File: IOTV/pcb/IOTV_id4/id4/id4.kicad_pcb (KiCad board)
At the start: 2 copper layers, 35.6 x 53.3 mm, 7 parts, among them J1 Conn_01x04, J2 Conn_01x03, U1 WeMos_D1_mini

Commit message: pcb id4
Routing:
- net Net-(D1-K): track 7.18 -> 8.08 mm

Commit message: pcb id4
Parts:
- removed D1, D2, D3, D4: LED, LED_THT:LED_D2.0mm_W4.8mm_H2.5mm_FlatTop
- removed J1: Conn_01x04, Jumper:tht_jumper_x4-2.54mm
- removed J2: Conn_01x03, Jumper:tht_jumper_x3-2.54mm
- removed U1: WeMos_D1_mini, Module:WEMOS_D1_mini_light
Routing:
- net GND: track 82.1 -> 0.00 mm
- net 5V: track 62.9 -> 0.00 mm
- net BTN3: track 31.1 -> 0.00 mm
- net BTN2: track 28.7 -> 0.00 mm
- net ADC: track 27.7 -> 0.00 mm
- net BTN1: track 26.6 -> 0.00 mm
- net BTN4: track 25.0 -> 0.00 mm
- net Net-(D1-K): track 8.08 -> 0.00 mm
- net Net-(D4-K): track 6.16 -> 0.00 mm
- net Net-(D2-K): track 6.16 -> 0.00 mm
- net Net-(D3-K): track 5.08 -> 0.00 mm
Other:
- board outline removed
- board text removed: "5V"
- board text removed: "ADC"
- board text removed: "BT1"
- board text removed: "BT2"
- board text removed: "BT3"
- board text removed: "BT4"
- board text removed: "GND"
- board text removed: "IOTV_ID4"
- board text removed: "WeMos_D1_mini"

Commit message: pcb src id4
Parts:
- added Q1: S8050, Package_TO_SOT_THT:TO-92_Inline, F.Cu at (52.5, 2.75)
- added Q10: S8050, Package_TO_SOT_THT:TO-92_Inline, F.Cu at (59.0, 20.1)
- added Q11: S8050, Package_TO_SOT_THT:TO-92_Inline, F.Cu at (59.0, 25.9)
- added Q12: S8050, Package_TO_SOT_THT:TO-92_Inline, F.Cu at (59.0, 31.7)
- added Q13: S8050, Package_TO_SOT_THT:TO-92_Inline, F.Cu at (65.6, 2.75)
- added Q14: S8050, Package_TO_SOT_THT:TO-92_Inline, F.Cu at (65.6, 8.54)
- added Q15: S8050, Package_TO_SOT_THT:TO-92_Inline, F.Cu at (65.6, 14.3)
- added Q2: S8050, Package_TO_SOT_THT:TO-92_Inline, F.Cu at (52.5, 8.54)
- added Q3: S8050, Package_TO_SOT_THT:TO-92_Inline, F.Cu at (52.5, 14.3)
- added Q4: S8050, Package_TO_SOT_THT:TO-92_Inline, F.Cu at (52.5, 20.1)
- added Q5: S8050, Package_TO_SOT_THT:TO-92_Inline, F.Cu at (52.5, 25.9)
- added Q6: S8050, Package_TO_SOT_THT:TO-92_Inline, F.Cu at (52.5, 31.7)
- added Q7: S8050, Package_TO_SOT_THT:TO-92_Inline, F.Cu at (59.0, 2.75)
- added Q8: S8050, Package_TO_SOT_THT:TO-92_Inline, F.Cu at (59.0, 8.54)
- added Q9: S8050, Package_TO_SOT_THT:TO-92_Inline, F.Cu at (59.0, 14.3)
- added U1: ESP32-WROOM-32, RF_Module:ESP32-WROOM-32, F.Cu at (24.0, 30.8)

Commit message: pcb id4
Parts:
- added D0: LED_RGBA, LED_THT:LED_D5.0mm-4_RGB, F.Cu at (86.4, 64.8)
- added D1: LED_RGBA, LED_THT:LED_D5.0mm-4_RGB, F.Cu at (146.1, 64.8)
- added D2: LED_RGBA, LED_THT:LED_D5.0mm-4_RGB, F.Cu at (209.6, 64.8)
- added D3: LED_RGBA, LED_THT:LED_D5.0mm-4_RGB, F.Cu at (209.6, 127.5)
- added D4: LED_RGBA, LED_THT:LED_D5.0mm-4_RGB, F.Cu at (88.9, 131.4)
- added R1: 100, Resistor_SMD:R_1206_3216Metric, F.Cu at (131.1, 56.5)
- added R10: 100, Resistor_SMD:R_1206_3216Metric, F.Cu at (152.9, 133.9)
- added R11: 100, Resistor_SMD:R_1206_3216Metric, F.Cu at (152.9, 137.2)
- added R12: 100, Resistor_SMD:R_1206_3216Metric, F.Cu at (152.9, 140.5)
- added R13: 100, Resistor_SMD:R_1206_3216Metric, F.Cu at (152.9, 143.8)
- added R14: 100, Resistor_SMD:R_1206_3216Metric, F.Cu at (152.9, 147.1)
- added R15: 100, Resistor_SMD:R_1206_3216Metric, F.Cu at (152.9, 150.4)
- added R16: 150, Resistor_SMD:R_1206_3216Metric, F.Cu at (83.0, 72.6)
- added R17: 330, Resistor_SMD:R_1206_3216Metric, F.Cu at (86.8, 72.5)
- added R18: 100, Resistor_SMD:R_1206_3216Metric, F.Cu at (90.5, 72.5)
- added R19: 150, Resistor_SMD:R_1206_3216Metric, F.Cu at (158.6, 137.2)
- added R2: 100, Resistor_SMD:R_1206_3216Metric, F.Cu at (107.5, 70.9)
- added R20: 330, Resistor_SMD:R_1206_3216Metric, F.Cu at (158.6, 140.5)
- added R21: 100, Resistor_SMD:R_1206_3216Metric, F.Cu at (158.6, 143.8)
- added R22: 150, Resistor_SMD:R_1206_3216Metric, F.Cu at (158.6, 147.1)
- added R23: 330, Resistor_SMD:R_1206_3216Metric, F.Cu at (158.6, 150.4)
- added R24: 100, Resistor_SMD:R_1206_3216Metric, F.Cu at (158.6, 153.7)
- added R25: 150, Resistor_SMD:R_1206_3216Metric, F.Cu at (164.2, 130.6)
- added R26: 330, Resistor_SMD:R_1206_3216Metric, F.Cu at (164.2, 133.9)
- added R27: 100, Resistor_SMD:R_1206_3216Metric, F.Cu at (164.2, 137.2)
- added R28: 150, Resistor_SMD:R_1206_3216Metric, F.Cu at (164.2, 140.5)
- added R29: 330, Resistor_SMD:R_1206_3216Metric, F.Cu at (164.2, 143.8)
- added R3: 100, Resistor_SMD:R_1206_3216Metric, F.Cu at (124.5, 50.5)
- added R30: 100, Resistor_SMD:R_1206_3216Metric, F.Cu at (164.2, 147.1)
- added R4: 100, Resistor_SMD:R_1206_3216Metric, F.Cu at (147.3, 140.5)
- added R5: 100, Resistor_SMD:R_1206_3216Metric, F.Cu at (147.3, 143.8)
- added R6: 100, Resistor_SMD:R_1206_3216Metric, F.Cu at (147.3, 147.1)
- added R7: 100, Resistor_SMD:R_1206_3216Metric, F.Cu at (147.3, 150.4)
- added R8: 100, Resistor_SMD:R_1206_3216Metric, F.Cu at (147.3, 153.7)
- added R9: 100, Resistor_SMD:R_1206_3216Metric, F.Cu at (152.9, 130.6)
- added SW1: SW_Push, Button_Switch_SMD:SW_SPST_TL3342, F.Cu at (116.8, 117.5)
- added SW2: SW_Push, Button_Switch_SMD:SW_SPST_TL3342, F.Cu at (106.7, 117.5)
- added SW3: SW_Push, Button_Switch_SMD:SW_SPST_TL3342, F.Cu at (95.8, 117.5)
- added U2: DFR0299, import:MODULE_DFR0299, F.Cu at (105.4, 88.9)
- added dynamic1: Speaker, Jumper:SolderJumper-2_P1.3mm_Open_Pad1.0x1.5mm, F.Cu at (125.7, 75.5)
- Q1, Q10, Q11, Q12, Q13, Q14, Q15, Q2, Q3, Q4, Q5, Q6, Q7, Q8, Q9: footprint Package_TO_SOT_THT:TO-92_Inline -> Package_TO_SOT_SMD:SOT-23
- U1: value ESP32-WROOM-32 -> ESP32_DevKit_V1_DOIT; footprint RF_Module:ESP32-WROOM-32 -> kicad:esp32_devkit_v1_doit
- moved U1 174.3 mm to (191.8, 78.1)
- moved Q7 150.4 mm to (137.2, 131.2)
- moved Q13 149.5 mm to (142.1, 131.2)
- moved Q8 149.2 mm to (137.2, 135.7)
- moved Q14 148.4 mm to (142.1, 135.7)
- moved Q9 148.1 mm to (137.2, 140.1)
- moved Q4 147.8 mm to (132.3, 144.6)
- moved Q15 147.2 mm to (142.1, 140.1)
- moved Q10 147.0 mm to (137.2, 144.6)
- moved Q5 146.7 mm to (132.3, 149.0)
- moved Q11 145.8 mm to (137.2, 149.0)
- moved Q6 145.6 mm to (132.3, 153.5)
- moved Q12 144.7 mm to (137.2, 153.5)
- moved Q1 80.7 mm to (83.0, 77.5), turned to 90 degrees
- moved Q2 76.9 mm to (86.7, 77.4), turned to 90 degrees
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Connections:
- U1 pad 1: Net-(U1-GND-Pad1) -> unconnected-(U1-EN-Pad1)
- U1 pad 10: GPIO_25 -> GPIO_27
- U1 pad 11: unconnected-(U1-IO26-Pad11) -> GPIO_14
- U1 pad 12: unconnected-(U1-IO27-Pad12) -> GPIO_12
- U1 pad 13: unconnected-(U1-IO14-Pad13) -> GPIO_13
- U1 pad 14: unconnected-(U1-IO12-Pad14) -> GND
- U1 pad 15: Net-(U1-GND-Pad1) -> VCC_5
- U1 pad 17: unconnected-(U1-SHD/SD2-Pad17) -> GND
- U1 pad 18: unconnected-(U1-SWP/SD3-Pad18) -> GPIO_15
- U1 pad 19: unconnected-(U1-SCS/CMD-Pad19) -> GPIO_2
- U1 pad 2: unconnected-(U1-VDD-Pad2) -> GPIO_36
- U1 pad 20: unconnected-(U1-SCK/CLK-Pad20) -> GPIO_4
- U1 pad 21: unconnected-(U1-SDO/SD0-Pad21) -> GPIO_16
- U1 pad 22: unconnected-(U1-SDI/SD1-Pad22) -> GPIO_17
- U1 pad 23: unconnected-(U1-IO15-Pad23) -> GPIO_5
- U1 pad 24: unconnected-(U1-IO2-Pad24) -> GPIO_18
- U1 pad 25: unconnected-(U1-IO0-Pad25) -> GPIO_19
- U1 pad 26: unconnected-(U1-IO4-Pad26) -> GPIO_21
- U1 pad 29: unconnected-(U1-IO5-Pad29) -> GPIO_22
- U1 pad 3: unconnected-(U1-EN-Pad3) -> GPIO_39
- U1 pad 30: unconnected-(U1-IO18-Pad30) -> GPIO_23
- U1 pad 4: unconnected-(U1-SENSOR_VP-Pad4) -> GPIO_34
- U1 pad 5: unconnected-(U1-SENSOR_VN-Pad5) -> GPIO_35
- U1 pad 6: unconnected-(U1-IO34-Pad6) -> GPIO_32
- U1 pad 7: unconnected-(U1-IO35-Pad7) -> GPIO_33
- U1 pad 8: GPIO_32 -> unconnected-(U1-IO25-Pad8)
- U1 pad 9: GPIO_33 -> unconnected-(U1-IO26-Pad9)
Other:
- board text added: "Speaker 50 mm 8 Om"

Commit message: PCB - ID4
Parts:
- removed D0: LED_RGBA, LED_THT:LED_D5.0mm-4_RGB
- added D5: LED_RGBA, LED_THT:LED_D5.0mm-4_RGB, F.Cu at (120.7, 120.7)
- added REF**: KiCad-Logo2_5mm_SilkScreen, Symbol:KiCad-Logo2_5mm_SilkScreen, F.Cu at (167.0, 107.4)
- Q1, Q10, Q11, Q12, Q13, Q14, Q15, Q2, Q3, Q4, Q5, Q6, Q7, Q8, Q9, R10, R11, R12, R15, R18, R19, R20, R21, R24, R25, R26, R27, R3, R30, R4, R5, R6, R9: moved to B.Cu
- R1, R13, R7: value 100 -> 150; moved to B.Cu
- R14, R2, R8: value 100 -> 330; moved to B.Cu
- R16, R22, R28: value 150 -> 100; moved to B.Cu
- R17, R23, R29: value 330 -> 100; moved to B.Cu
- moved D4 129.3 mm to (217.8, 120.7), turned to 0 degrees
- moved R16 108.3 mm to (191.2, 76.5), turned to 180 degrees
- moved R17 99.3 mm to (186.0, 76.5), turned to 180 degrees
- moved R18 90.3 mm to (180.8, 76.5), turned to 180 degrees
- moved Q12 89.1 mm to (172.5, 71.7), turned to 90 degrees
- moved R15 88.4 mm to (181.0, 66.5), turned to -90 degrees
- moved R14 87.1 mm to (186.0, 66.5), turned to -90 degrees
- moved R13 86.3 mm to (191.2, 66.5), turned to -90 degrees
- moved Q11 83.1 mm to (167.5, 71.7), turned to 90 degrees
- moved R6 81.6 mm to (153.8, 65.8), turned to 90 degrees
- moved Q9 81.5 mm to (181.0, 71.4), turned to 90 degrees
- moved Q8 80.7 mm to (186.0, 71.4), turned to 90 degrees
- moved Q7 80.6 mm to (191.2, 71.4), turned to 90 degrees
- moved R21 78.7 mm to (170.5, 66.0), turned to -90 degrees
- moved R24 78.7 mm to (172.5, 76.2), turned to 180 degrees
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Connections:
- R1 pad 1: GPIO_15 -> Net-(D1-RK)
- R1 pad 2: Net-(Q1-B) -> Net-(Q1-C)
- R10 pad 2: Net-(Q10-B) -> Net-(Q4-B)
- R11 pad 2: Net-(Q11-B) -> Net-(Q5-B)
- R12 pad 2: Net-(Q12-B) -> Net-(Q6-B)
- R13 pad 1: GPIO_12 -> Net-(D3-RK)
- R13 pad 2: Net-(Q13-B) -> Net-(Q7-C)
- R14 pad 1: GPIO_14 -> Net-(D3-GK)
- R14 pad 2: Net-(Q14-B) -> Net-(Q8-C)
- R15 pad 1: GPIO_27 -> Net-(D3-BK)
- R15 pad 2: Net-(Q15-B) -> Net-(Q9-C)
- R16 pad 1: Net-(D0-RK) -> GPIO_18
- R16 pad 2: Net-(Q1-C) -> Net-(Q7-B)
- R17 pad 1: Net-(D0-GK) -> GPIO_19
- R17 pad 2: Net-(Q2-C) -> Net-(Q8-B)
- R18 pad 1: Net-(D0-BK) -> GPIO_21
- R18 pad 2: Net-(Q3-C) -> Net-(Q9-B)
- R19 pad 1: Net-(D1-RK) -> Net-(D2-RK)
- R19 pad 2: Net-(Q4-C) -> Net-(Q10-C)
- R2 pad 1: GPIO_2 -> Net-(D1-GK)
- R2 pad 2: Net-(Q2-B) -> Net-(Q3-C)
- R20 pad 1: Net-(D1-GK) -> Net-(D2-GK)
- R20 pad 2: Net-(Q5-C) -> Net-(Q11-C)
- R21 pad 1: Net-(D1-BK) -> Net-(D2-BK)
- R21 pad 2: Net-(Q6-C) -> Net-(Q12-C)
- R22 pad 1: Net-(D2-RK) -> GPIO_33
- R22 pad 2: Net-(Q7-C) -> Net-(Q10-B)
- R23 pad 1: Net-(D2-GK) -> GPIO_32
- R23 pad 2: Net-(Q8-C) -> Net-(Q11-B)
- R24 pad 1: Net-(D2-BK) -> GPIO_5
- R24 pad 2: Net-(Q9-C) -> Net-(Q12-B)
- R25 pad 1: Net-(D3-RK) -> Net-(D5-RK)
- R25 pad 2: Net-(Q10-C) -> Net-(Q13-C)
- R26 pad 1: Net-(D3-GK) -> Net-(D5-GK)
- R26 pad 2: Net-(Q11-C) -> Net-(Q14-C)
- R27 pad 1: Net-(D3-BK) -> Net-(D5-BK)
- R27 pad 2: Net-(Q12-C) -> Net-(Q15-C)
- R28 pad 1: Net-(D4-RK) -> GPIO_12
- R28 pad 2: Net-(Q13-C) -> Net-(Q13-B)
- R29 pad 1: Net-(D4-GK) -> GPIO_14
- R29 pad 2: Net-(Q14-C) -> Net-(Q14-B)
- R3 pad 1: GPIO_4 -> Net-(D1-BK)
- R3 pad 2: Net-(Q3-B) -> Net-(Q2-C)
- R30 pad 1: Net-(D4-BK) -> GPIO_27
- R30 pad 2: Net-(Q15-C) -> Net-(Q15-B)
- R4 pad 1: GPIO_33 -> GPIO_15
- R4 pad 2: Net-(Q4-B) -> Net-(Q1-B)
- R5 pad 1: GPIO_32 -> GPIO_2
- R5 pad 2: Net-(Q5-B) -> Net-(Q3-B)
- R6 pad 1: GPIO_5 -> GPIO_4
- R6 pad 2: Net-(Q6-B) -> Net-(Q2-B)
- R7 pad 1: GPIO_18 -> Net-(D4-RK)
- R7 pad 2: Net-(Q7-B) -> Net-(Q4-C)
- R8 pad 1: GPIO_19 -> Net-(D4-GK)
- R8 pad 2: Net-(Q8-B) -> Net-(Q5-C)
- R9 pad 1: GPIO_21 -> Net-(D4-BK)
- R9 pad 2: Net-(Q9-B) -> Net-(Q6-C)
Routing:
- net GPIO_17: track 0.00 -> 122.4 mm
- net GPIO_16: track 0.00 -> 122.3 mm
- net GPIO_4: track 0.00 -> 85.5 mm, vias 0 -> 2
- net GPIO_35: track 0.00 -> 84.0 mm, vias 0 -> 2
- net GPIO_39: track 0.00 -> 82.4 mm, vias 0 -> 2
- net GPIO_2: track 0.00 -> 82.0 mm, vias 0 -> 2
- net GPIO_34: track 0.00 -> 77.3 mm, vias 0 -> 2
- net GPIO_15: track 0.00 -> 76.9 mm, vias 0 -> 2
- net GPIO_22: track 0.00 -> 64.4 mm
- net GPIO_36: track 0.00 -> 60.8 mm
- net GPIO_21: track 0.00 -> 60.0 mm
- net GPIO_19: track 0.00 -> 58.0 mm
- net GPIO_5: track 0.00 -> 54.5 mm, vias 0 -> 1
- net GPIO_23: track 0.00 -> 53.7 mm
- net GPIO_18: track 0.00 -> 52.6 mm
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- added copper zone on B.Cu, net GND
- added copper zone on F.Cu, net VCC_5
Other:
- board outline added: 109.2 x 73.7 mm
- board text added: "-+"
- board text added: "IOTV ID-4"
- board text added: "Speaker 50mm 8OM"
- board text added: "rev. 1.0"
- board text removed: "Speaker 50 mm 8 Om"

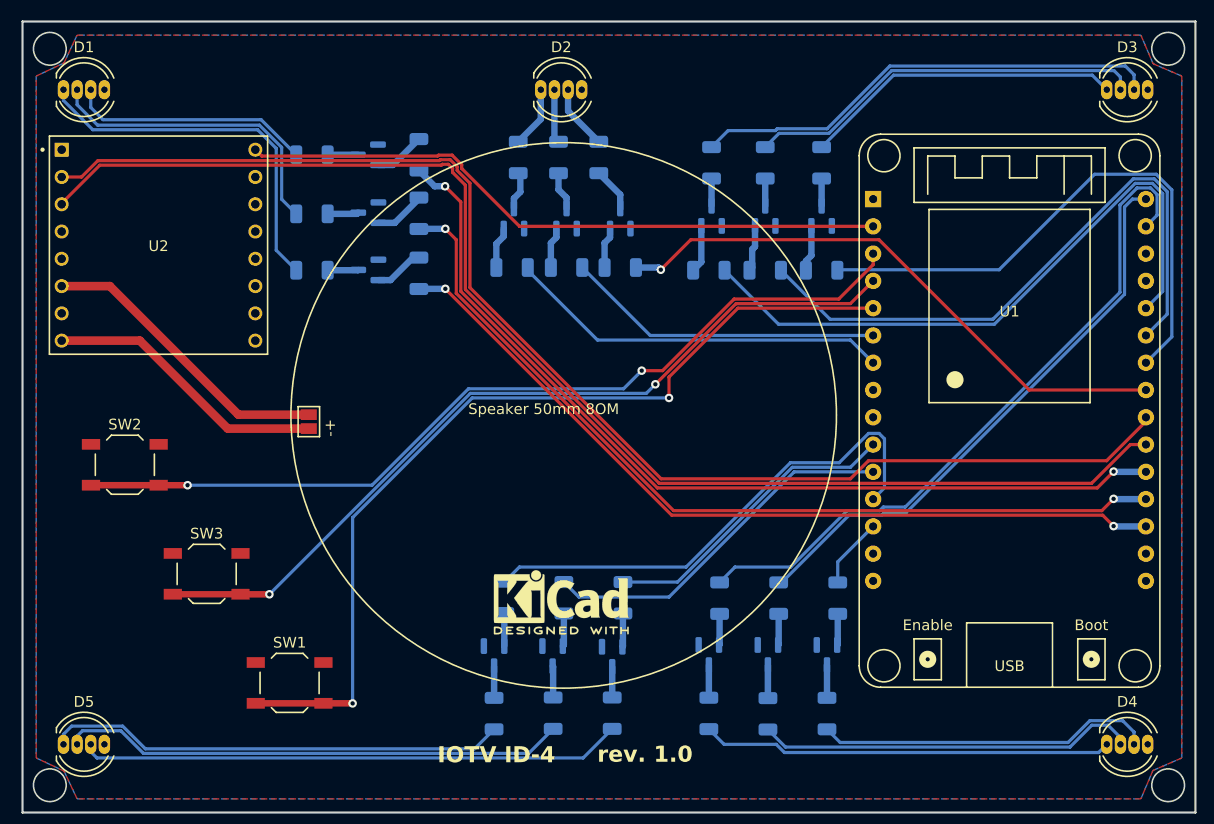
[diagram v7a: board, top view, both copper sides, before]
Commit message: pcb id4 - rezonit OK
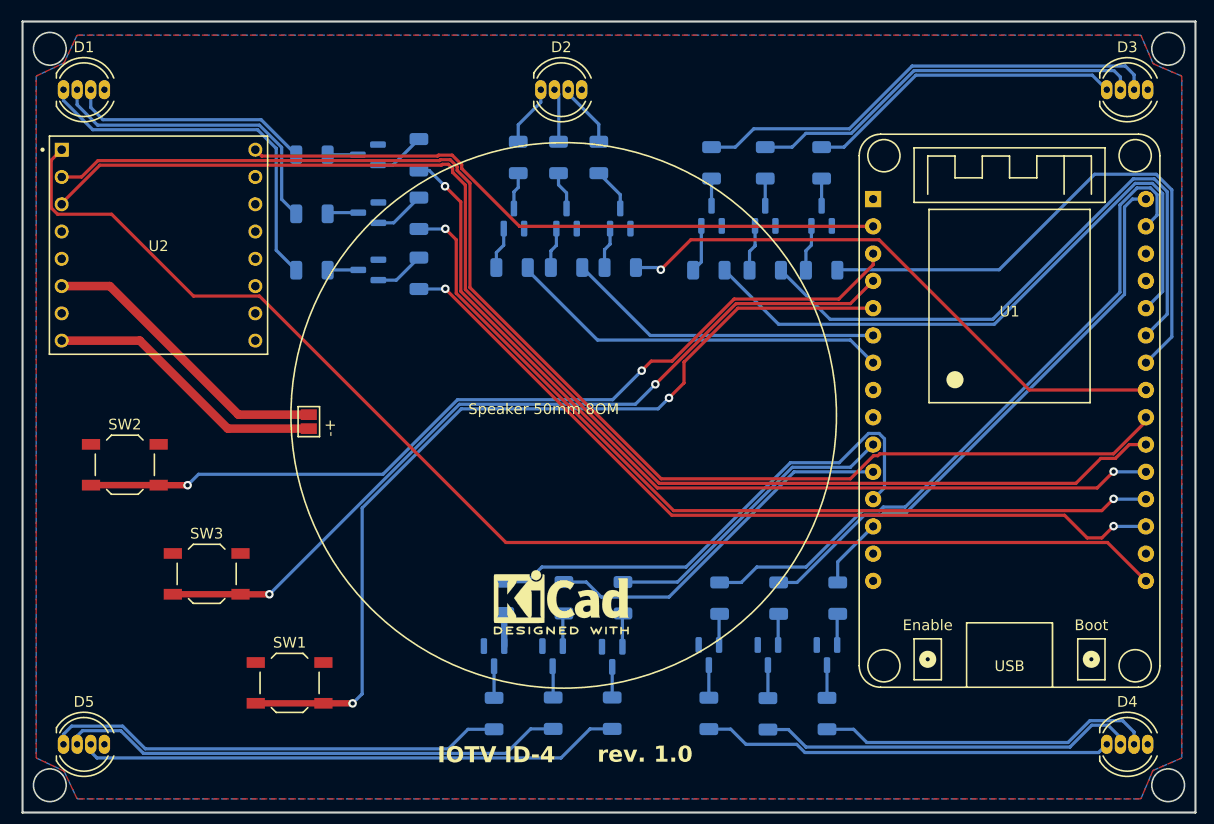
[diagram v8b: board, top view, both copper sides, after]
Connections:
- U1 pad 16: unconnected-(U1-3V3-Pad16) -> VCC_3.3
- U2 pad 1: VCC_5 -> VCC_3.3
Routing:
- net VCC_3.3: track 0.00 -> 122.2 mm
- net GPIO_15: track 76.9 -> 77.8 mm
